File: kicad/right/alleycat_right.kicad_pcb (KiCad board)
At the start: 2 copper layers, 134 x 128 mm, 115 parts, among them J1 Conn_01x04_Male, J2 USB_C_Receptacle_USB2.0, SW1 SW_Push, U1 nRF52840_holyiot_18010, U2 TP4056, U3 DW01A, U4 FS8205, U5 SRV05-4, U6 XC6206PxxxMR

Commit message: uhh wicked
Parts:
- added D45: D_Small, Diode_SMD:D_SOD-123, B.Cu at (37.0, 36.0)
- moved J2 101.3 mm to (-98.0, 15.6), turned to 180 degrees
- moved D39 79.3 mm to (-60.5, 111.0)
- moved D46 70.9 mm to (22.0, 44.0)
- moved C3 69.6 mm to (-62.7, 85.8)
- moved R8 69.6 mm to (-67.2, 85.8)
- moved R3 69.6 mm to (-72.5, 83.9)
- moved U6 69.6 mm to (-63.4, 82.1)
- moved U4 69.6 mm to (-57.9, 84.3)
- moved C8 67.2 mm to (-11.0, 78.0)
- moved D44 66.5 mm to (27.0, 110.0), turned to 0 degrees
- moved L1 66.0 mm to (-89.0, 56.0)
- moved F1 58.5 mm to (-43.0, 65.0)
- moved C1 58.4 mm to (-62.0, 88.8)
- moved R10 58.4 mm to (-70.9, 88.7)
- moved R6 58.4 mm to (-66.5, 88.8)
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- renumbered D45 to Dr
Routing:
- net row_4: track 163.9 -> 121.2 mm
- net col_6: track 37.4 -> 0.00 mm
- net row_0: track 91.8 -> 118.3 mm
- net row_1: track 130.4 -> 123.7 mm
- net row_2: track 130.4 -> 123.7 mm
- net row_5: track 135.0 -> 128.4 mm
- net row_3: track 127.8 -> 121.7 mm
- net Net-(D46-Pad2): track 0.00 -> 3.36 mm
- net Net-(D42-Pad2): track 4.77 -> 8.07 mm
- net Net-(D45-Pad2): track 5.68 -> 7.82 mm
- net col_1: track 111.2 -> 109.8 mm
- net col_5: track 129.8 -> 131.1 mm
- net col_0: track 110.7 -> 109.5 mm
- net col_2: track 110.7 -> 109.5 mm
- net col_4: track 114.3 -> 115.3 mm
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
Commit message: swag
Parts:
- U1: footprint E73-2G4M08S1C:E73-2G4M08S1C -> marbastlib-various:nRF52840_holyiot_18010
- moved U5 83.2 mm to (19.0, 102.0)
- moved J2 76.2 mm to (-22.0, 20.6)
- moved D40 65.0 mm to (18.0, 117.0)
- moved D41 65.0 mm to (32.0, 117.0)
- moved D42 65.0 mm to (18.0, 103.0)
- moved D46 65.0 mm to (22.0, 109.0)
- moved Dr 65.0 mm to (32.0, 103.0)
- moved S1 65.0 mm to (25.0, 110.0)
- moved U6 64.8 mm to (1.00, 89.0)
- moved U4 62.9 mm to (3.00, 100.0)
- moved F1 42.2 mm to (-2.00, 75.0)
- moved SW1 39.0 mm to (-11.0, 127.0)
- moved D44 23.9 mm to (7.00, 97.0)
- moved U2 8.06 mm to (31.0, 102.0)
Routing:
- added copper zone on B.Cu, net GND

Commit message: nya
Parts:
- moved MX36 0.07 mm to (23.1, 131.0)

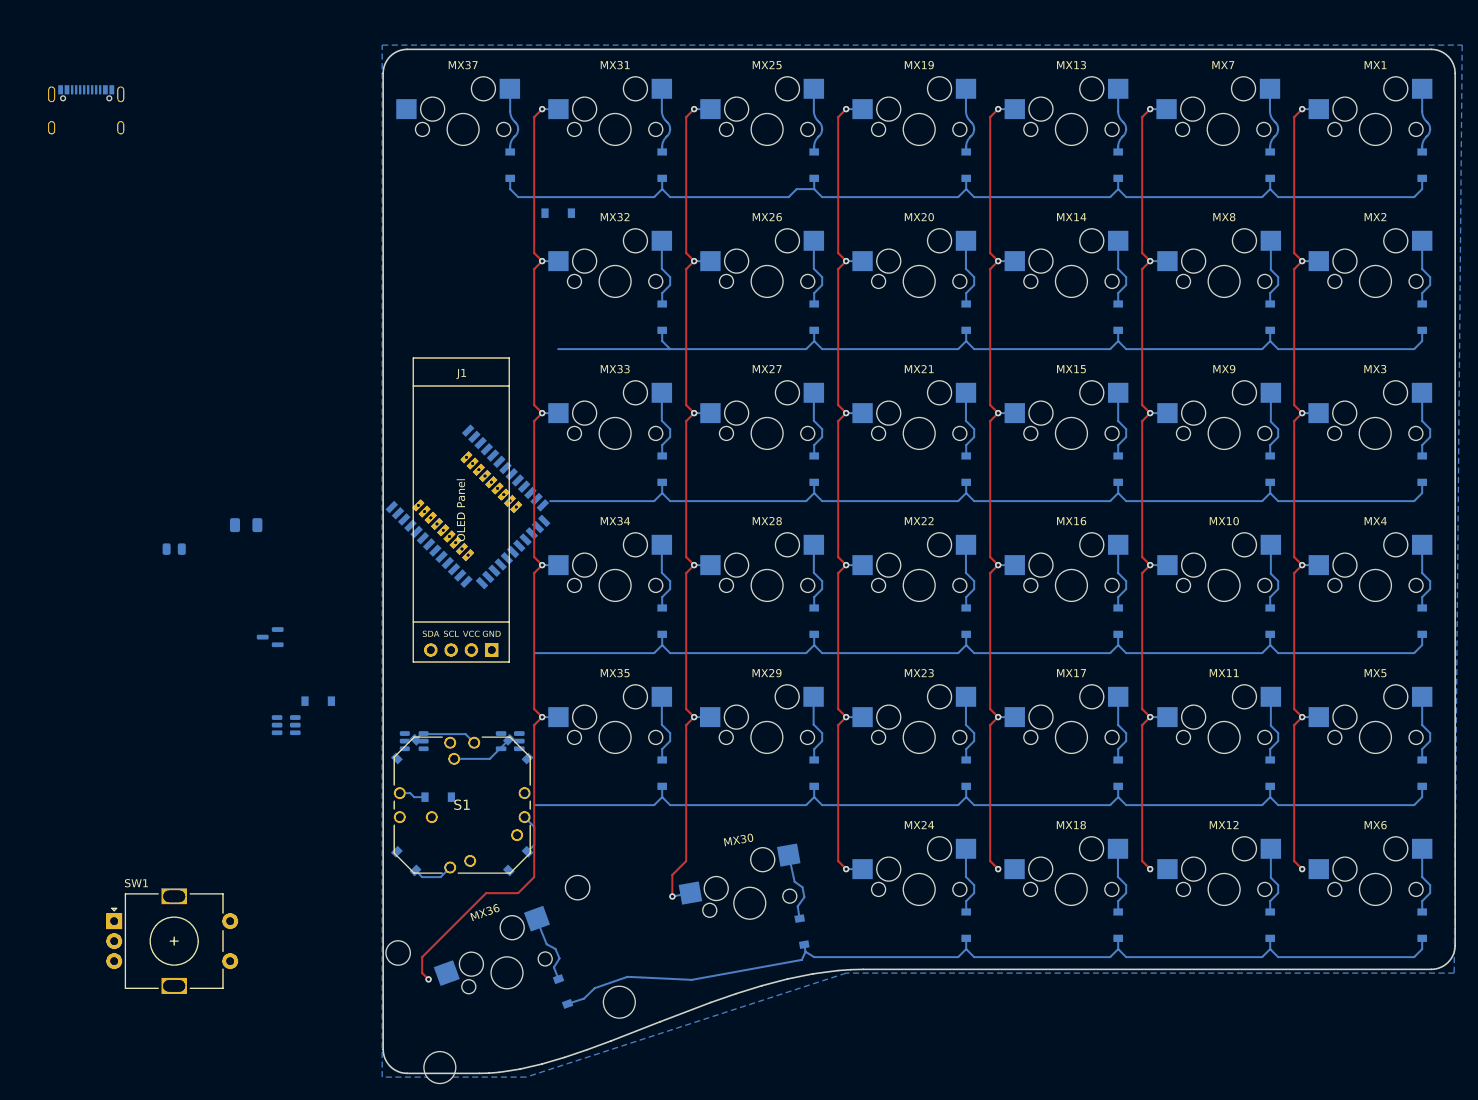
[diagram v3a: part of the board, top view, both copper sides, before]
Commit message: did the right allignment
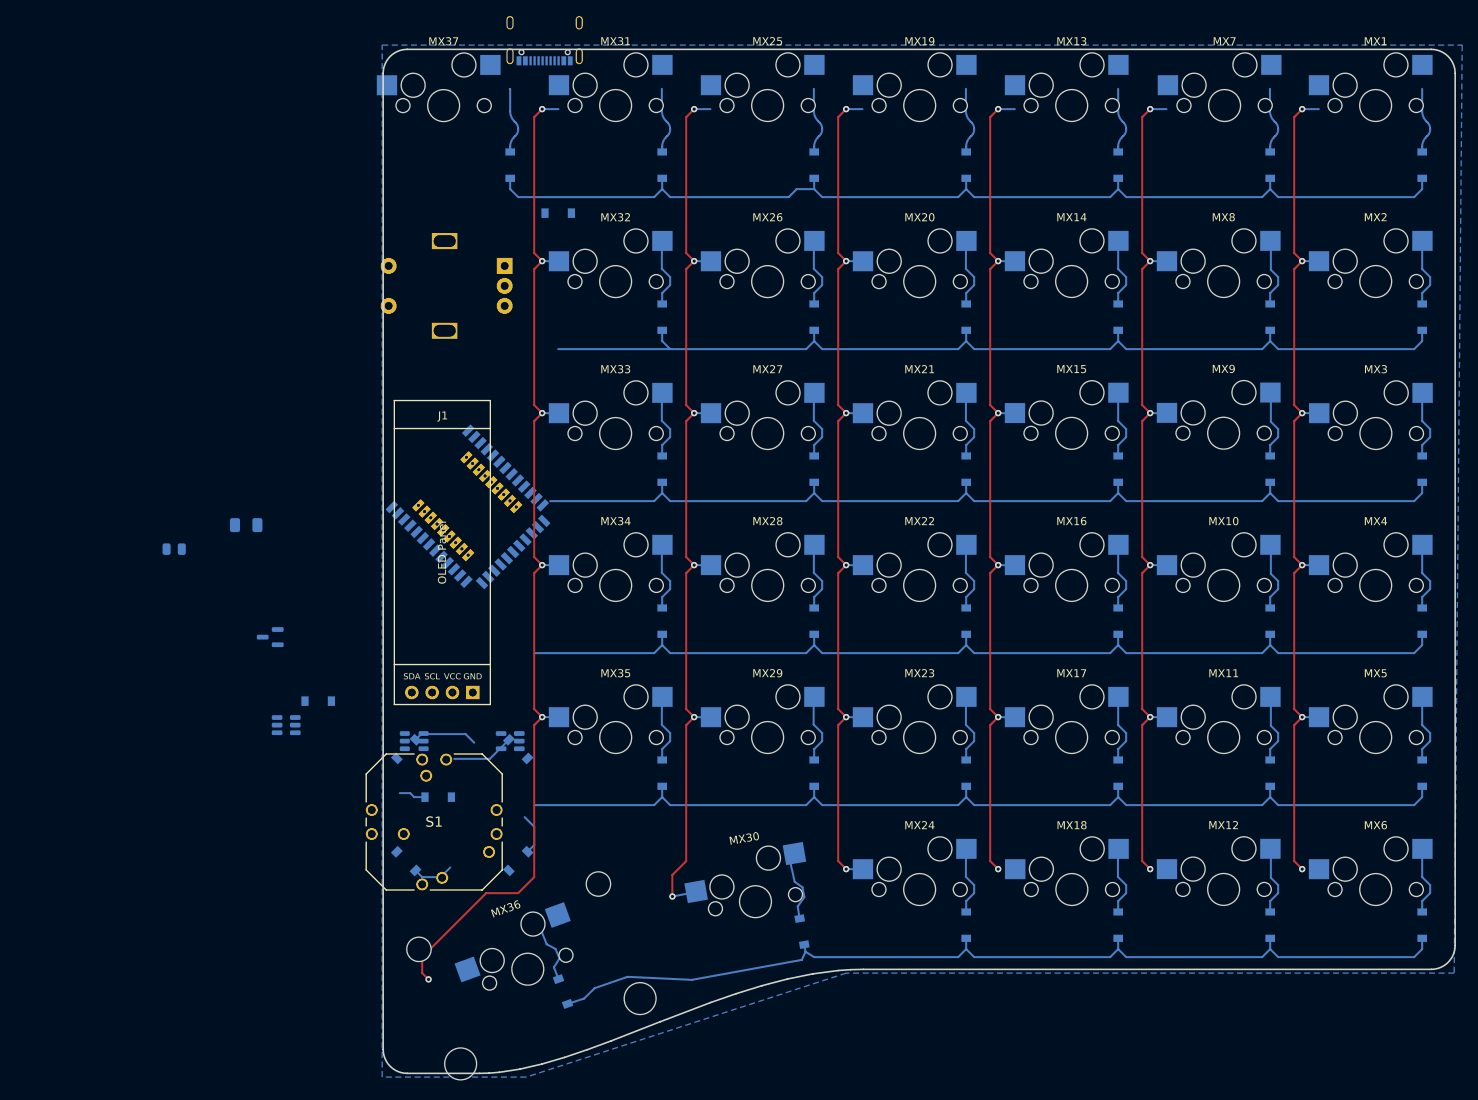
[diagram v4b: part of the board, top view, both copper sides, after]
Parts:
- SW1: moved to B.Cu
- moved SW1 88.6 mm to (22.8, 45.1), turned to 180 degrees
- moved J2 57.4 mm to (35.3, 17.0), turned to 0 degrees
- moved J1 5.81 mm to (28.5, 59.4)
- moved S1 4.09 mm to (21.5, 112.1)
- moved MX37 3.85 mm to (15.6, 20.0)
- moved MX7 2.99 mm to (113.2, 20.0)
- moved MX25 2.99 mm to (56.1, 20.0)
- moved MX31 2.99 mm to (37.1, 20.0)
- moved MX19 2.99 mm to (75.1, 20.0)
- moved MX13 2.99 mm to (94.1, 20.0)
- moved MX1 2.99 mm to (132.1, 20.0)
- moved MX36 2.64 mm to (25.7, 130.5)
- moved MX30 0.74 mm to (54.2, 120.8)
- moved MX29 0.10 mm to (56.1, 99.0)
- moved MX18 0.08 mm to (94.1, 118.0)
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
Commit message: a
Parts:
- added SW2: RotaryEncoder_Switch, Keebio-Parts:RotaryEncoder_Alps_EC11E-Switch_Vertical_H20mm, F.Cu at (-12.0, 118.0)
- SW1: footprint Keebio-Parts:RotaryEncoder_Alps_EC11E-Switch_Vertical_H20mm -> Keebio-Parts:SW_SPST_TL3342
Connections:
- J1 pad 2: vbus -> +5V
- U1 pad 44: (no net) -> unconnected-(U1-Pad44)
- U1 pad 45: (no net) -> unconnected-(U1-Pad45)
- U1 pad 46: (no net) -> unconnected-(U1-Pad46)
- U1 pad 47: (no net) -> unconnected-(U1-Pad47)
- U1 pad 48: (no net) -> unconnected-(U1-Pad48)
- U1 pad 49: (no net) -> unconnected-(U1-Pad49)
- U1 pad 50: (no net) -> unconnected-(U1-Pad50)
- U1 pad 51: (no net) -> unconnected-(U1-Pad51)
- U1 pad 52: (no net) -> unconnected-(U1-Pad52)
- U1 pad 53: (no net) -> unconnected-(U1-Pad53)
- U1 pad 54: (no net) -> unconnected-(U1-Pad54)
- U1 pad 55: (no net) -> unconnected-(U1-Pad55)
- U5 pad 3: unconnected-(U5-Pad3) -> D-
- U5 pad 4: D- -> unconnected-(U5-Pad4)
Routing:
- net Net-(D42-Pad2): track 8.07 -> 0.00 mm
- net D+: track 0.00 -> 8.07 mm
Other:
- board size 134 x 128 mm -> 139.8 x 136.9 mm
